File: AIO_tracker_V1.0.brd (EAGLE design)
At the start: 46.8 x 94 mm, 69 parts, among them J1 EDGE_ICSP, Q1 MOSFET-PCHANNELSMD, U2 USD-SOCKETNEW, X1 SMA-142-0701-881/886, Y2 16MHz

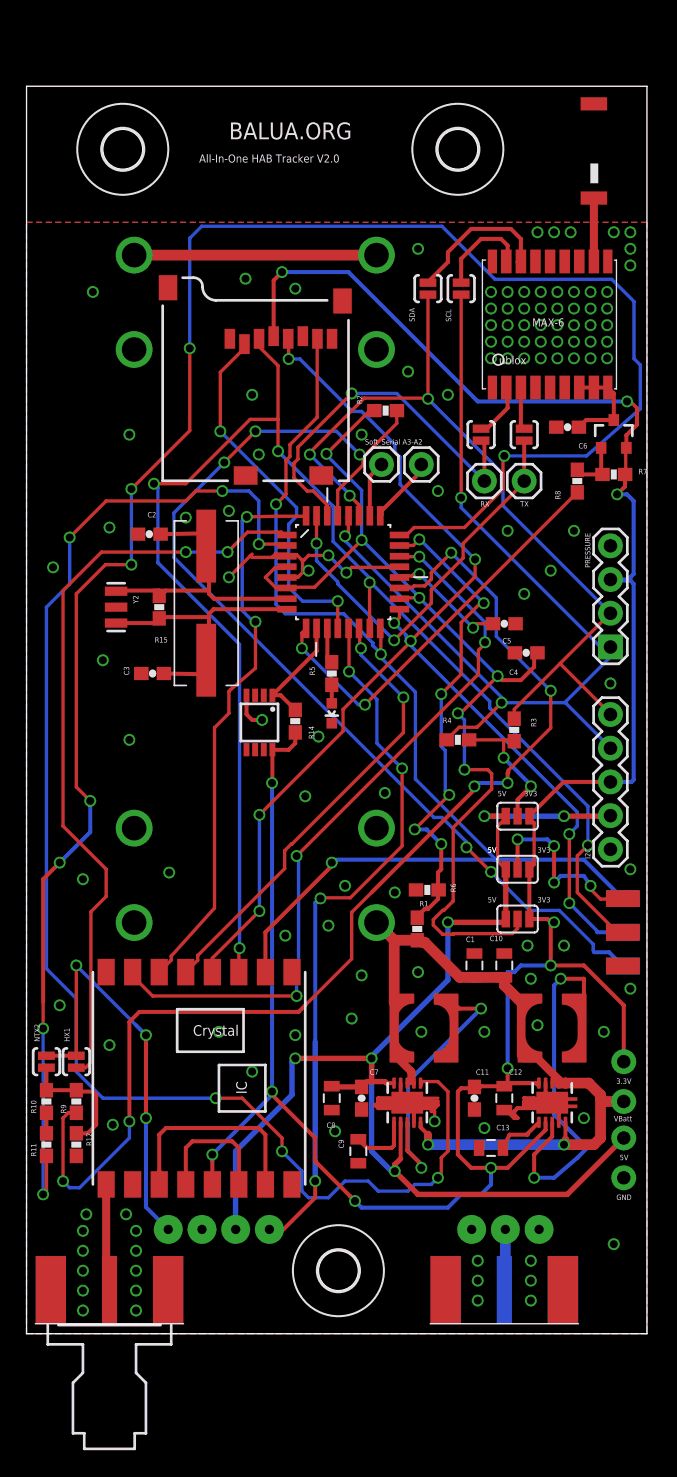
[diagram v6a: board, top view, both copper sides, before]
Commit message: changed holes to match the stencil
changed holes to match the stencil sticks (2.5mm) and the 10mm spacing
between them
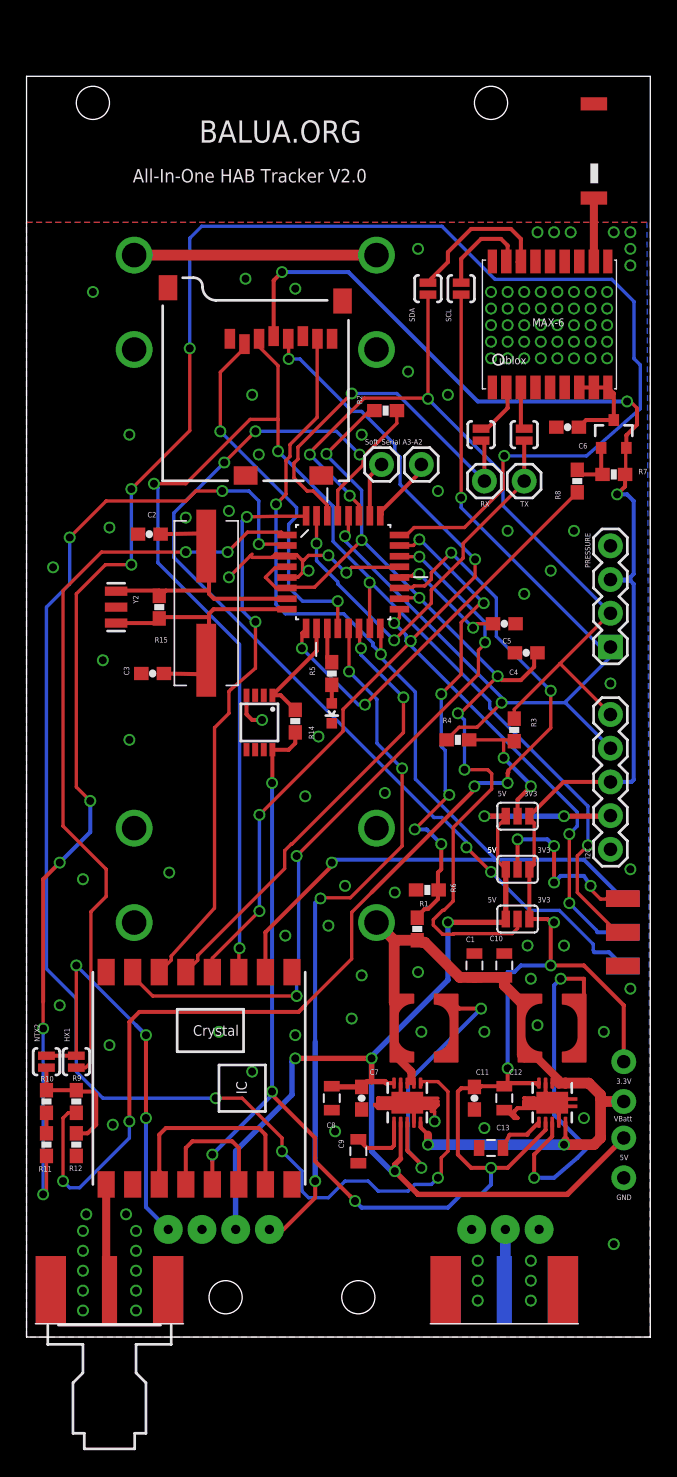
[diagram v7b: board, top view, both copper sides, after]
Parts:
- removed U$10, U$11, U$5: (no value), holes:3,0
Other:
- board size 46.8 x 94 mm -> 47 x 95 mm
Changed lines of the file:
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@@
 <setting verticaltext="up"/>
 </settings>
-<grid distance="0.25" unitdist="mm" unit="mm" style="lines" multiple="1" display="yes" altdistance="0.025" altunitdist="inch" altunit="inch"/>
+<grid distance="0.1" unitdist="mm" unit="mm" style="lines" multiple="1" display="yes" altdistance="0.025" altunitdist="inch" altunit="inch"/>
 <layers>
 <layer number="1" name="Top" color="4" fill="1" visible="yes" active="yes"/>
@@
 <board>
 <plain>
-<wire x1="-1" y1="-16.75" x2="45.75" y2="-16.75" width="0" layer="20"/>
-<wire x1="45.75" y1="-16.75" x2="45.75" y2="77.25" width="0" layer="20"/>
-<wire x1="45.75" y1="77.25" x2="-1" y2="77.25" width="0" layer="20"/>
-<wire x1="-1" y1="77.25" x2="-1" y2="-16.75" width="0" layer="20"/>
-<text x="14.25" y="73.25" size="1.27" layer="25">BALUA.ORG</text>
-<text x="12" y="71.5" size="0.6096" layer="25" font="vector" ratio="25">All-In-One HAB Tracker V2.0</text>
+<wire x1="-1" y1="-17" x2="46" y2="-17" width="0" layer="20"/>
+<wire x1="46" y1="-17" x2="46" y2="78" width="0" layer="20"/>
+<wire x1="46" y1="78" x2="-1" y2="78" width="0" layer="20"/>
+<wire x1="-1" y1="78" x2="-1" y2="-17" width="0" layer="20"/>
+<text x="12" y="73" size="1.6764" layer="25">BALUA.ORG</text>
+<text x="7" y="70" size="1.016" layer="25" font="vector" ratio="25">All-In-One HAB Tracker V2.0</text>
 <text x="24.5" y="50.25" size="0.4064" layer="25" font="vector" ratio="25">Soft_Serial A3-A2</text>
 <text x="43.25" y="-0.75" size="0.4064" layer="25" font="vector" ratio="25" distance="25">VBatt</text>
@@
 <rectangle x1="41.75" y1="7.5" x2="42.75" y2="9.75" layer="32"/>
 <rectangle x1="-0.5" y1="7.5" x2="0.5" y2="9.75" layer="32"/>
+<hole x="4" y="76" drill="2.5"/>
+<hole x="34" y="76" drill="2.5"/>
+<hole x="14" y="-14" drill="2.5"/>
+<hole x="24" y="-14" drill="2.5"/>
 </plain>
 <attributes>
@@
 <element name="SJ2" library="SparkFun-Passives" package="SJ_2S-NO" value="SOLDERJUMPERNO" x="2.75" y="3.75" smashed="yes" rot="R270"/>
 <element name="SJ4" library="SparkFun-Passives" package="SJ_2S-NO" value="SOLDERJUMPERNO" x="0.5" y="3.75" smashed="yes" rot="R270"/>
-<element name="U$5" library="holes" package="3,0" value="" x="31.5" y="72.5"/>
-<element name="U$10" library="holes" package="3,0" value="" x="6.25" y="72.5"/>
-<element name="U$11" library="holes" package="3,0" value="" x="22.5" y="-12"/>
-<element name="R9" library="SparkFun-Passives" package="0603-RES" value="22k" x="2.75" y="0.75" rot="R90"/>
-<element name="R10" library="SparkFun-Passives" package="0603-RES" value="22k" x="0.5" y="0.75" rot="R90"/>
-<element name="R11" library="SparkFun-Passives" package="0603-RES" value="4.7k" x="0.5" y="-2.5" rot="R90"/>
-<element name="R12" library="SparkFun-Passives" package="0603-RES" value="10k" x="2.75" y="-2.5" rot="R270"/>
+<element name="R9" library="SparkFun-Passives" package="0603-RES" value="22k" x="2.75" y="0.75" smashed="yes" rot="R90">
+<attribute name="NAME" x="2.461" y="2.312" size="0.4064" layer="25" font="vector" ratio="25"/>
+</element>
+<element name="R10" library="SparkFun-Passives" package="0603-RES" value="22k" x="0.5" y="0.75" smashed="yes" rot="R90">
+<attribute name="NAME" x="0.061" y="2.262" size="0.4064" layer="25" font="vector" ratio="25"/>
+</element>
+<element name="R11" library="SparkFun-Passives" package="0603-RES" value="4.7k" x="0.5" y="-2.5" smashed="yes" rot="R90">
+<attribute name="NAME" x="-0.089" y="-4.538" size="0.4064" layer="25" font="vector" ratio="25"/>
+</element>
+<element name="R12" library="SparkFun-Passives" package="0603-RES" value="10k" x="2.75" y="-2.5" smashed="yes" rot="R270">
+<attribute name="NAME" x="2.211" y="-4.488" size="0.4064" layer="25" font="vector" ratio="25"/>
+</element>
 </elements>
 <signals>
@@
 <vertex x="-1" y="67"/>
 <vertex x="45.75" y="67"/>
-<vertex x="45.75" y="-16.75"/>
-<vertex x="-1" y="-16.75"/>
+<vertex x="46" y="-17"/>
+<vertex x="-1" y="-17"/>
 </polygon>
 <polygon width="0.4064" layer="1" isolate="0.4064">
 <vertex x="-1" y="67"/>
-<vertex x="45.75" y="67"/>
-<vertex x="45.75" y="-16.75"/>
-<vertex x="-1" y="-16.75"/>
+<vertex x="46" y="67"/>
+<vertex x="46" y="-17"/>
+<vertex x="-1" y="-17"/>
 </polygon>
 <contactref element="U$1" pad="6_V_BCKP"/>

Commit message: removed jumpers and ntx2 support
removed jumpers and ntx2 support
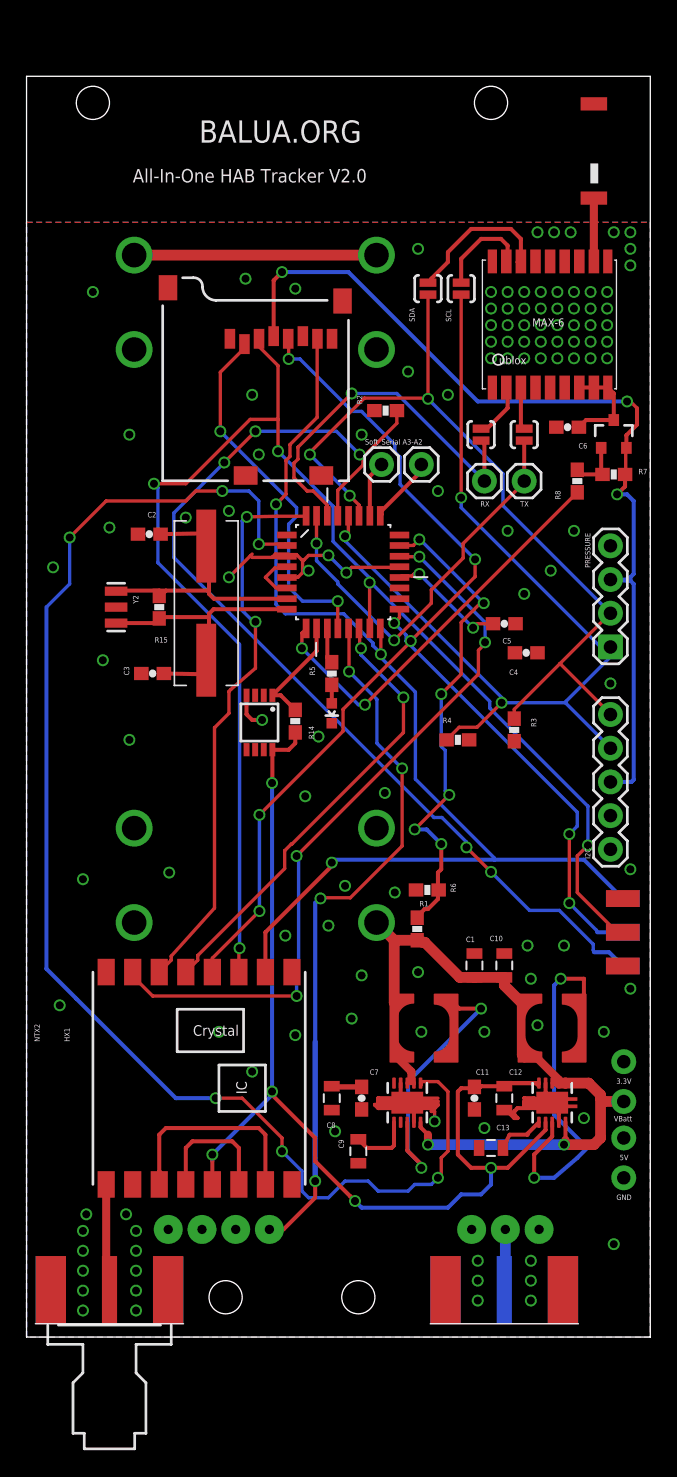
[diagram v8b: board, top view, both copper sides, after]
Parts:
- removed JP1: JUMPER-3SMD, SparkFun-Passives:SJ_3
- removed JP2, JP3: (no value), SparkFun-Passives:SJ_3
- removed R10, R9: 22k, SparkFun-Passives:0603-RES
- removed R11: 4.7k, SparkFun-Passives:0603-RES
- removed R12: 10k, SparkFun-Passives:0603-RES
- removed SJ2, SJ4: SOLDERJUMPERNO, SparkFun-Passives:SJ_2S-NO
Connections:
- removed net N$14: JP3.2, R3.2, R4.2
- removed net N$17: R10.2, R12.1, R9.2, SJ4.2
- removed net N$18: R10.1, R11.2
- removed net N$8: C4.1, JP1.2, R2.2, U1.18, U1.4, U1.6
- removed net N$9: J1.2, JP2.2
- removed net TXDHX1NX2: SJ2.1, SJ4.1, U$3.TXD
- net 3.3V: now also C4.1, J1.2, R2.2, R3.2, R4.2, U1.18, U1.4, U1.6; no longer JP1.1, JP2.1, JP3.1
- net 5V: no longer JP1.3, JP2.3, JP3.3
- net GND: no longer R12.2
- net HX1: now also U$3.TXD; no longer SJ2.2
- net MARK: no longer R11.1
- net SPACE: no longer R9.1
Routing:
- net MARK: track 149.8 -> 0.00 mm, vias 8 -> 0
- net 5V: track 96.9 -> 2.41 mm, vias 6 -> 0
- net SPACE: track 88.1 -> 0.00 mm, vias 6 -> 0
- net N$8: track 75.8 -> 0.00 mm, vias 6 -> 0
- net HX1: track 57.5 -> 0.11 mm, vias 2 -> 0
- net 3.3V: track 203.5 -> 162.8 mm, vias 11 -> 8
- net TXDHX1NX2: track 31.8 -> 0.00 mm, vias 3 -> 0
- net N$9: track 14.4 -> 0.00 mm, vias 4 -> 0
- net N$14: track 11.9 -> 0.00 mm, vias 2 -> 0
- net N$17: track 9.61 -> 0.00 mm
- net EN_POW_5V: track 107.1 -> 103.9 mm
- net N$18: track 1.55 -> 0.00 mm
- net GND: vias 124 -> 122
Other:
- board text removed: "3V3"
- board text removed: "5V"
